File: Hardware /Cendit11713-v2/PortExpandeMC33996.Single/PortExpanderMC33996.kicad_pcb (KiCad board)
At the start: 2 copper layers, 12 parts, among them J1 DEBUG_CONN, P1 VIKING_HEADER_9P, P2 VIKING_HEADER_9P, U1 MC33996EKR2

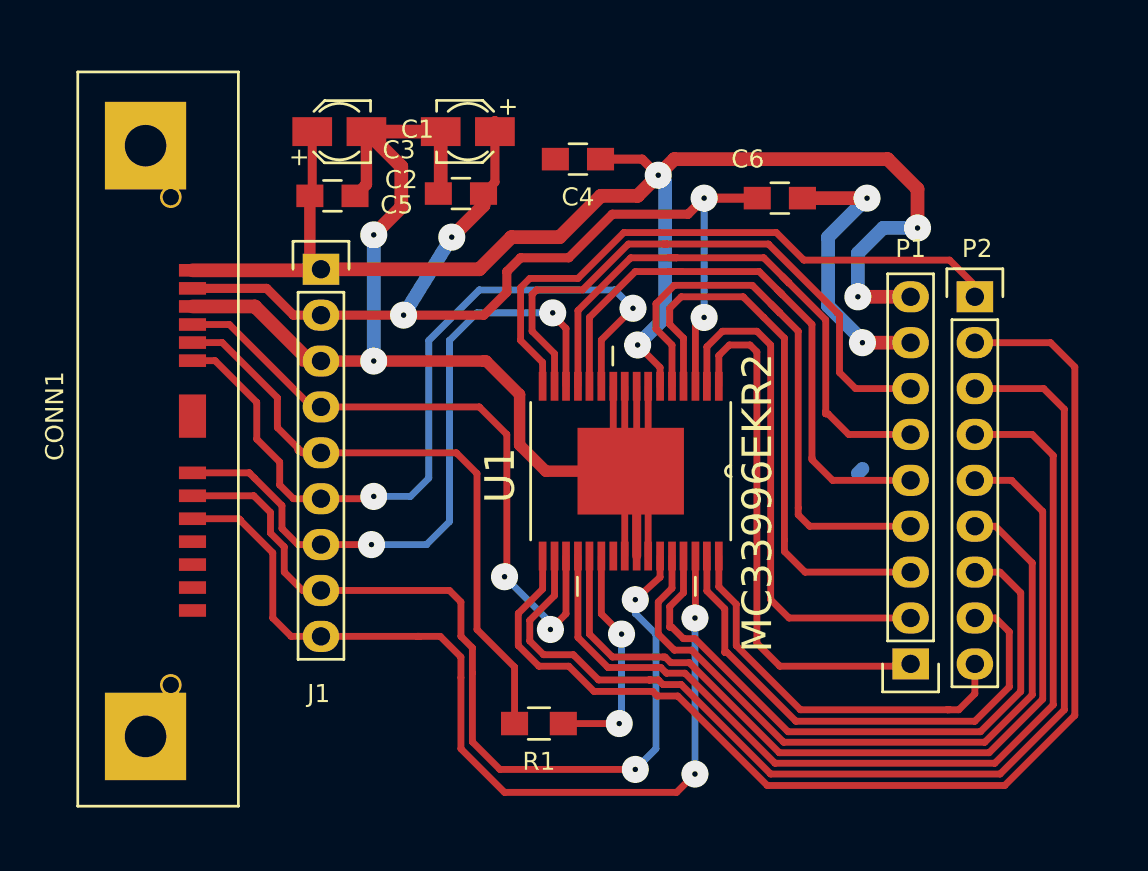
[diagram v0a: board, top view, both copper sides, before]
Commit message: Trabajo en Cendit11713
  - Revision de esquematicos + PCBs
  - Generacion de archivos Gerber
  - CapacitiveKeyboard -> edicion PCB
  - Inicia PCB GpibPortExpander
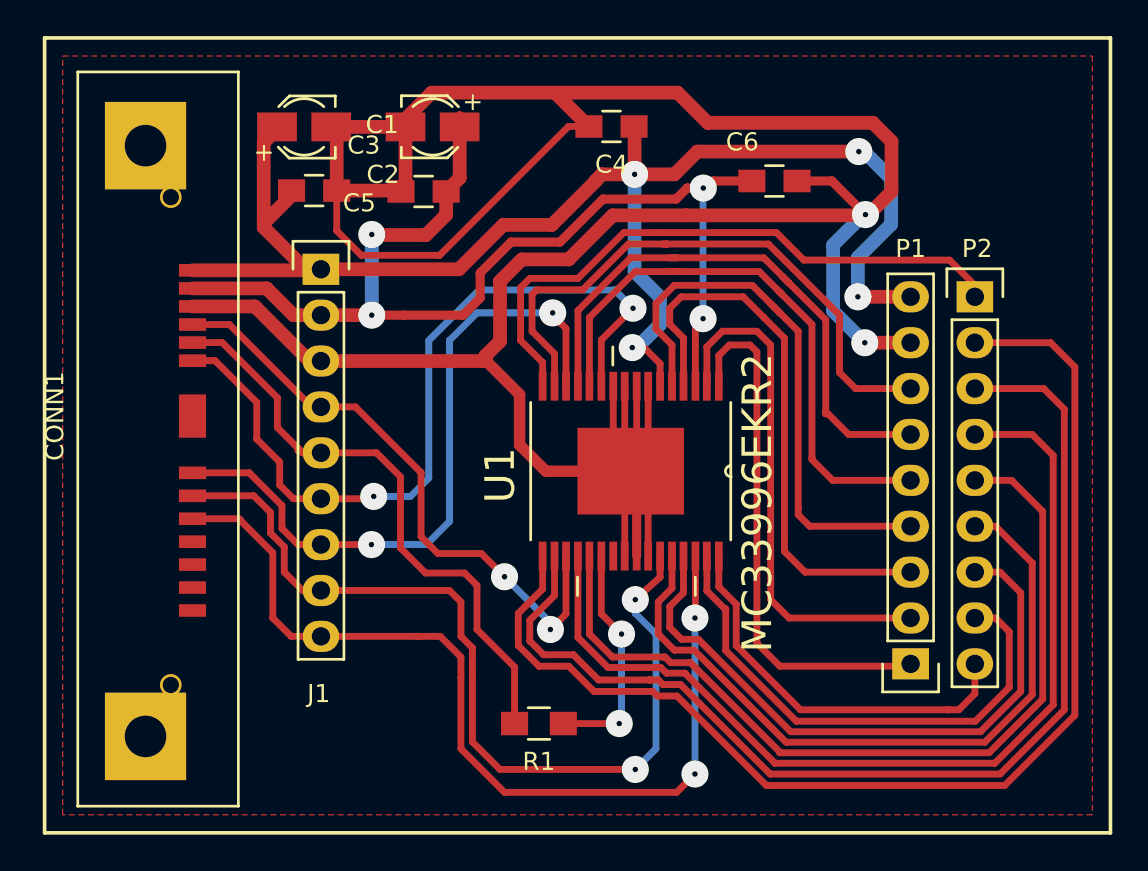
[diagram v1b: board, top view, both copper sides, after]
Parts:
- moved C4 2.59 mm to (122.4, 82.9)
- moved C5 2.07 mm to (112.0, 86.5)
- moved C1 1.97 mm to (105.4, 82.9)
- moved C3 1.97 mm to (112.5, 82.9)
- moved C2 1.05 mm to (105.9, 86.5)
- moved C6 0.99 mm to (131.4, 85.9)
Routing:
- net GNDPWR: track 109.0 -> 179.7 mm, vias 4 -> 2
- net VCC: track 59.0 -> 62.3 mm
- net /MOSI: track 36.2 -> 33.7 mm
- net VPP: track 79.5 -> 81.9 mm
- net /MISO: track 34.9 -> 33.5 mm
- added copper zone on F.Cu, net GNDPWR

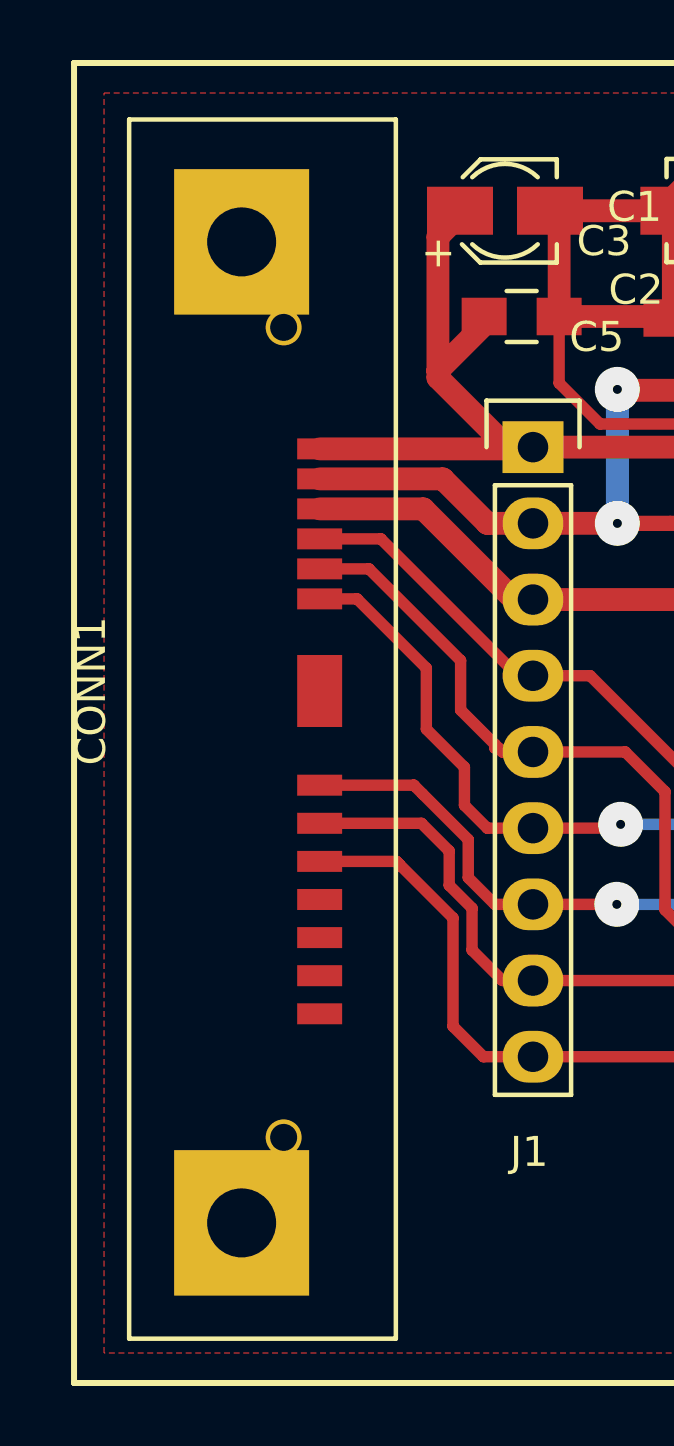
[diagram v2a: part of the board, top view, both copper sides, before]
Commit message: En Cendit11713 edicion de esquematicos + revision PCBs
  - Edicion de esquematicos tarjeta madre
  - Revision de PCBs corrección de footprints
  - Descarga de footprints + creacion lib simbolos: RTC + sensor temp/hum
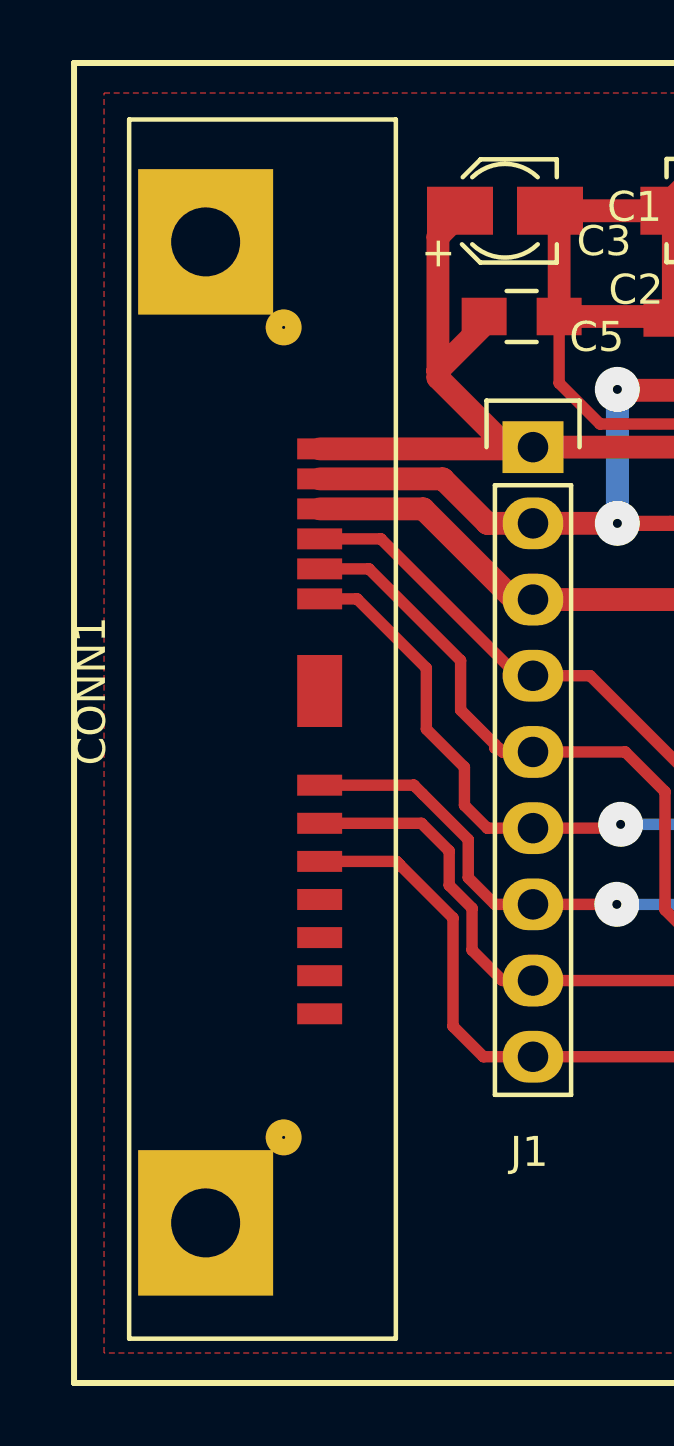
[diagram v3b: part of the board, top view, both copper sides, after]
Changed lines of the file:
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@@
-(kicad_pcb (version 4) (host pcbnew 4.0.6-e0-6349~53~ubuntu14.04.1)
+(kicad_pcb (version 4) (host pcbnew 4.0.5+dfsg1-4~bpo8+1)
   (general
     (links 56)
     (no_connects 0)
-    (area 90.592 70.02 164.143936 122.100001)
+    (area 0 0 0 0)
     (thickness 1.6)
     (drawings 6)
@@
     )
   )
-  (module CenditFootprints:SLIMLINE_SATA_PLUG_7P_6P (layer F.Cu)
-    (at 99.187 98.933 270)
-    (fp_text reference CONN1 (at 0 7.62 270) (layer F.SilkS)
-      (effects (font (size 1 1) (thickness 0.15)))
-    )
-    (fp_text value VIKING_SPI_BUS (at 1.397 -4.572 450) (layer F.Fab)
-      (effects (font (size 1 1) (thickness 0.15)))
-    )
-    (fp_line (start -19.05 6.35) (end 21.59 6.35) (layer F.SilkS) (width 0.15))
-    (fp_line (start 21.59 6.35) (end 21.59 -2.54) (layer F.SilkS) (width 0.15))
-    (fp_line (start 21.59 -2.54) (end -19.05 -2.54) (layer F.SilkS) (width 0.15))
-    (fp_line (start -19.05 -2.54) (end -19.05 6.35) (layer F.SilkS) (width 0.15))
-    (pad 14 smd rect (at 0 0 270) (size 2.4 1.5) (layers F.Cu F.Paste F.Mask))
-    (pad 12 smd rect (at 9.49 0 270) (size 0.7 1.5) (layers F.Cu F.Paste F.Mask))
-    (pad 11 smd rect (at 8.22 0 270) (size 0.7 1.5) (layers F.Cu F.Paste F.Mask))
-    (pad 13 smd rect (at 10.76 0 270) (size 0.7 1.5) (layers F.Cu F.Paste F.Mask))
-    (pad 10 smd rect (at 6.95 0 270) (size 0.7 1.5) (layers F.Cu F.Paste F.Mask))
-    (pad 9 smd rect (at 5.68 0 270) (size 0.7 1.5) (layers F.Cu F.Paste F.Mask)
-      (net 4 /PWM))
-    (pad 8 smd rect (at 4.41 0 270) (size 0.7 1.5) (layers F.Cu F.Paste F.Mask)
-      (net 5 //RESET))
-    (pad 7 smd rect (at 3.14 0 270) (size 0.7 1.5) (layers F.Cu F.Paste F.Mask)
-      (net 26 //CS))
-    (pad 6 smd rect (at -3.07 0 270) (size 0.7 1.5) (layers F.Cu F.Paste F.Mask)
-      (net 6 /SCLK))
-    (pad 5 smd rect (at -4.07 0 270) (size 0.7 1.5) (layers F.Cu F.Paste F.Mask)
-      (net 7 /MISO))
-    (pad 4 smd rect (at -5.07 0 270) (size 0.7 1.5) (layers F.Cu F.Paste F.Mask)
-      (net 8 /MOSI))
-    (pad 3 smd rect (at -6.07 0 270) (size 0.7 1.5) (layers F.Cu F.Paste F.Mask)
-      (net 1 GNDPWR))
-    (pad 2 smd rect (at -7.07 0 270) (size 0.7 1.5) (layers F.Cu F.Paste F.Mask)
-      (net 3 VCC))
-    (pad 1 smd rect (at -8.07 0 270) (size 0.7 1.5) (layers F.Cu F.Paste F.Mask)
-      (net 2 VPP))
-    (pad 17 thru_hole circle (at 14.88 1.2 270) (size 1.2 1.2) (drill 0.9) (layers *.Cu *.Mask))
-    (pad 16 thru_hole circle (at -12.12 1.2 270) (size 1.2 1.2) (drill 0.9) (layers *.Cu *.Mask))
-    (pad 15 thru_hole rect (at 17.73 2.6 270) (size 4.85 4.5) (drill 2.3) (layers *.Cu *.Mask))
-    (pad 14 thru_hole rect (at -14.97 2.6 270) (size 4.85 4.5) (drill 2.3) (layers *.Cu *.Paste *.Mask))
-  )
   (module Pin_Headers:Pin_Header_Straight_1x09 (layer F.Cu)
     (at 138.938 112.649 180)
@@
       (effects (font (size 1 1) (thickness 0.15)))
     )
-    (fp_text value DEBUG_CONN (at 2.921 16.256 90) (layer F.Fab)
+    (fp_text value DEBUG_CONN (at 2.921 9.779 90) (layer F.Fab)
       (effects (font (size 1 1) (thickness 0.15)))
     )
@@
     )
   )
+  (module CenditFootprints:SLIMLINE_SATA_PLUG_7P_6P (layer F.Cu)
+    (at 99.187 98.933 270)
+    (fp_text reference CONN1 (at 0 7.62 270) (layer F.SilkS)
+      (effects (font (size 1 1) (thickness 0.15)))
+    )
+    (fp_text value VIKING_SPI_BUS (at 0 -3.81 270) (layer F.Fab)
+      (effects (font (size 1 1) (thickness 0.15)))
+    )
+    (fp_line (start -19.05 6.35) (end 21.59 6.35) (layer F.SilkS) (width 0.15))
+    (fp_line (start 21.59 6.35) (end 21.59 -2.54) (layer F.SilkS) (width 0.15))
+    (fp_line (start 21.59 -2.54) (end -19.05 -2.54) (layer F.SilkS) (width 0.15))
+    (fp_line (start -19.05 -2.54) (end -19.05 6.35) (layer F.SilkS) (width 0.15))
+    (pad 14 smd rect (at 0 0 270) (size 2.4 1.5) (layers F.Cu F.Paste F.Mask))
+    (pad 12 smd rect (at 9.49 0 270) (size 0.7 1.5) (layers F.Cu F.Paste F.Mask))
+    (pad 11 smd rect (at 8.22 0 270) (size 0.7 1.5) (layers F.Cu F.Paste F.Mask))
+    (pad 13 smd rect (at 10.76 0 270) (size 0.7 1.5) (layers F.Cu F.Paste F.Mask))
+    (pad 10 smd rect (at 6.95 0 270) (size 0.7 1.5) (layers F.Cu F.Paste F.Mask))
+    (pad 9 smd rect (at 5.68 0 270) (size 0.7 1.5) (layers F.Cu F.Paste F.Mask)
+      (net 4 /PWM))
+    (pad 8 smd rect (at 4.41 0 270) (size 0.7 1.5) (layers F.Cu F.Paste F.Mask)
+      (net 5 //RESET))
+    (pad 7 smd rect (at 3.14 0 270) (size 0.7 1.5) (layers F.Cu F.Paste F.Mask)
+      (net 26 //CS))
+    (pad 6 smd rect (at -3.07 0 270) (size 0.7 1.5) (layers F.Cu F.Paste F.Mask)
+      (net 6 /SCLK))
+    (pad 5 smd rect (at -4.07 0 270) (size 0.7 1.5) (layers F.Cu F.Paste F.Mask)
+      (net 7 /MISO))
+    (pad 4 smd rect (at -5.07 0 270) (size 0.7 1.5) (layers F.Cu F.Paste F.Mask)
+      (net 8 /MOSI))
+    (pad 3 smd rect (at -6.07 0 270) (size 0.7 1.5) (layers F.Cu F.Paste F.Mask)
+      (net 1 GNDPWR))
+    (pad 2 smd rect (at -7.07 0 270) (size 0.7 1.5) (layers F.Cu F.Paste F.Mask)
+      (net 3 VCC))
+    (pad 1 smd rect (at -8.07 0 270) (size 0.7 1.5) (layers F.Cu F.Paste F.Mask)
+      (net 2 VPP))
+    (pad "" np_thru_hole circle (at 14.88 1.2 270) (size 1.2 1.2) (drill 0.1) (layers *.Cu *.Mask))
+    (pad "" np_thru_hole circle (at -12.12 1.2 270) (size 1.2 1.2) (drill 0.1) (layers *.Cu *.Mask))
+    (pad "" np_thru_hole rect (at 17.73 3.8 270) (size 4.85 4.5) (drill 2.3) (layers *.Cu *.Mask))
+    (pad "" np_thru_hole rect (at -14.97 3.8 270) (size 4.85 4.5) (drill 2.3) (layers *.Cu *.Mask))
+  )
   (dimension 41.870097 (width 0.3) (layer F.SilkS)

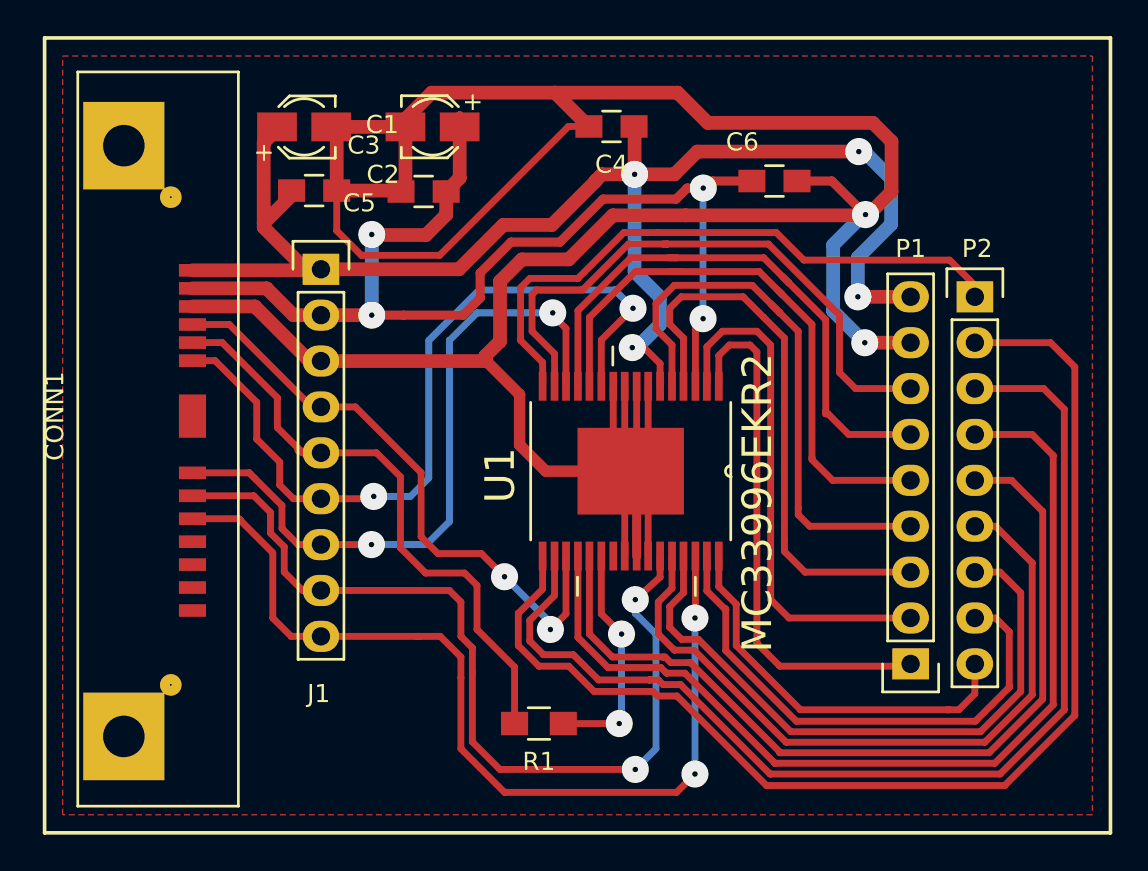
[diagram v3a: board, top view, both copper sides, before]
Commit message: En CenditLab.Reducido + Cendit11713
  - Para CenditLab vistas para Steps + fabrica de vistas ComponentViewfactory
  - En Cendit11713 revision PCB VikingPortExpander + Gerber
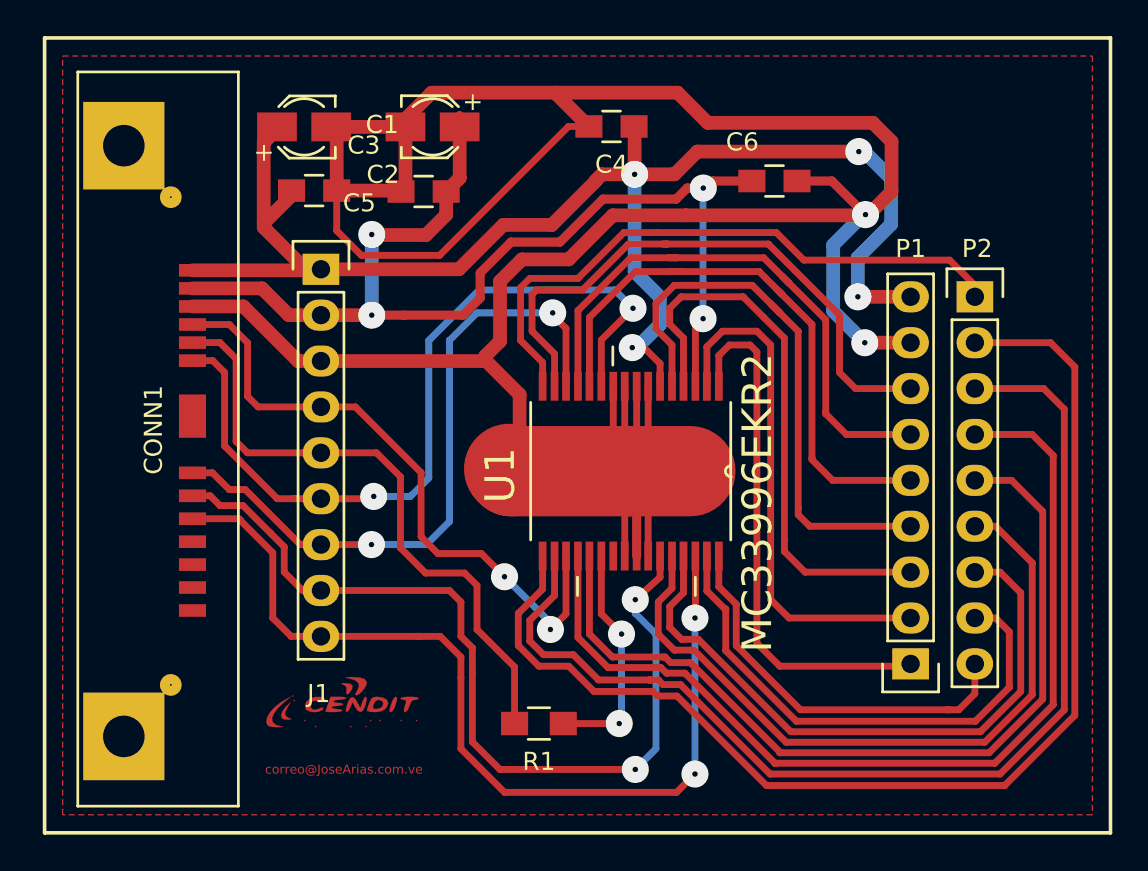
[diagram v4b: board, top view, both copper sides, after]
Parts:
- added G1: LOGO, CenditFootprints:CENDIT_LOGO_SOLDER, F.Cu at (108.3, 114.8)
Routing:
- net GNDPWR: track 179.7 -> 190.4 mm
- net /MISO: track 33.5 -> 35.8 mm
- net /MOSI: track 33.7 -> 36.0 mm
- net //CS: track 37.9 -> 37.1 mm
- net /SCLK: track 44.5 -> 45.2 mm
- net //RESET: track 49.8 -> 49.1 mm
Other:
- board text added: "correo@JoseArias.com.ve"
